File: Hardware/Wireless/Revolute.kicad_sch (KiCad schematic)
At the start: 52 parts, among them U1 BQ27441-G1, U2 Button, U2 nrf52833_qfn40, U3 AS5600, U4 AP2112K-3.3, U5 BQ24075RGT, X1 32.768 kHz, X2 32MHZ

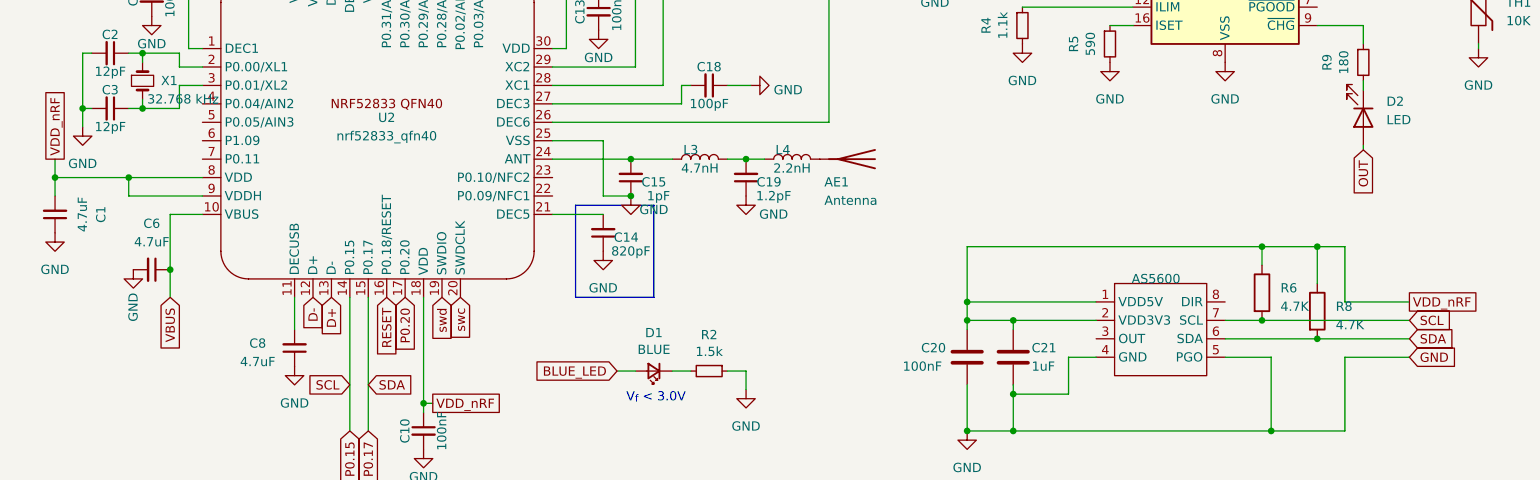
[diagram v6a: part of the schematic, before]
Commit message: fixed debugger datapin board, connected dir and out of as5600 to mcu
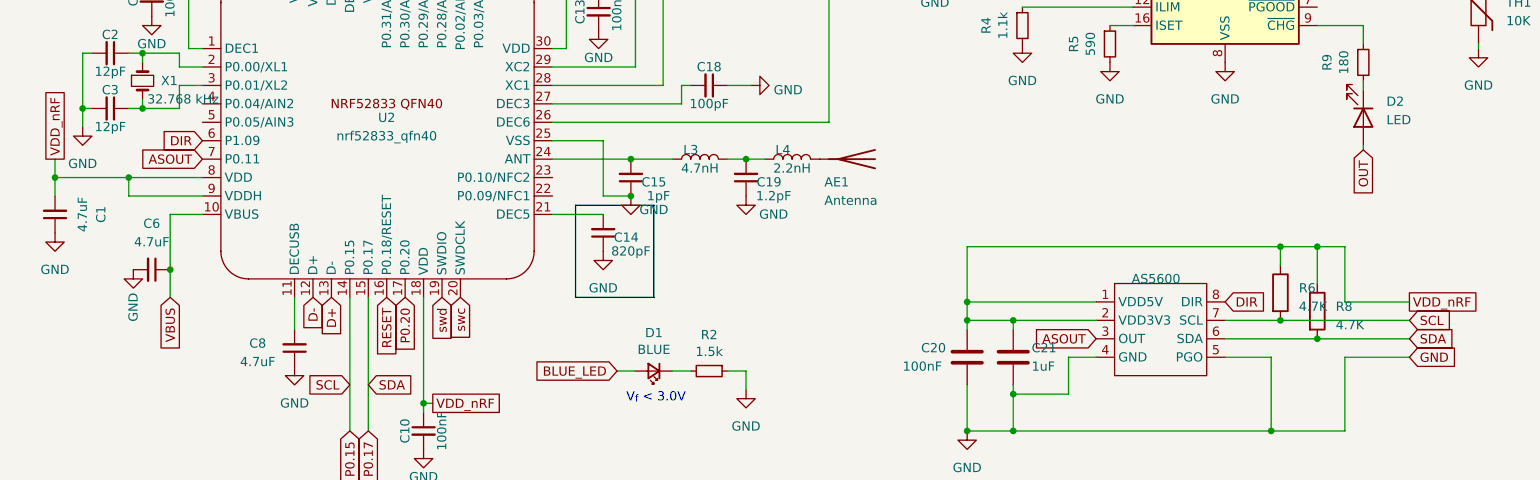
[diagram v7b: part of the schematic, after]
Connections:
- net DIR: now reaches U2.6 (P1.09)
- net DIR: now also U3.8 (DIR)
- net ASOUT: now reaches U2.7 (P0.11)
- net ASOUT: now also U3.3 (OUT)
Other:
- moved on the sheet: R6
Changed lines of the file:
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@@
   (junction (at 25.4 69.215) (diameter 0) (color 0 0 0 0)
   )
-  (junction (at 187.96 98.425) (diameter 0) (color 0 0 0 0)
-  )
   (junction (at 30.48 134.62) (diameter 0) (color 0 0 0 0)
   )
-  (junction (at 187.96 88.265) (diameter 0) (color 0 0 0 0)
+  (junction (at 190.5 98.425) (diameter 0) (color 0 0 0 0)
   )
   (junction (at 100.965 81.28) (diameter 0) (color 0 0 0 0)
@@
   (junction (at 21.59 78.74) (diameter 0) (color 0 0 0 0)
   )
+  (junction (at 190.5 88.265) (diameter 0) (color 0 0 0 0)
+  )
   (junction (at 198.12 140.335) (diameter 0) (color 0 0 0 0)
   )
@@
     (stroke (width 0) (type default))
   )
+  (wire (pts (xy 190.5 88.265) (xy 195.58 88.265))
+    (stroke (width 0) (type default))
+  )
   (wire (pts (xy 90.17 73.66) (xy 97.155 73.66))
     (stroke (width 0) (type default))
@@
     (stroke (width 0) (type default))
   )
-  (wire (pts (xy 187.96 88.265) (xy 187.96 90.805))
+  (wire (pts (xy 190.5 88.265) (xy 190.5 90.805))
     (stroke (width 0) (type default))
   )
@@
     (stroke (width 0) (type default))
   )
-  (wire (pts (xy 187.96 88.265) (xy 195.58 88.265))
-    (stroke (width 0) (type default))
-  )
   (wire (pts (xy 106.68 105.41) (xy 109.22 105.41))
     (stroke (width 0) (type solid))
@@
     (stroke (width 0) (type default))
   )
-  (wire (pts (xy 187.96 98.425) (xy 208.28 98.425))
+  (wire (pts (xy 182.88 98.425) (xy 190.5 98.425))
     (stroke (width 0) (type default))
   )
@@
     (stroke (width 0) (type default))
   )
+  (wire (pts (xy 190.5 98.425) (xy 208.28 98.425))
+    (stroke (width 0) (type default))
+  )
   (wire (pts (xy 73.66 109.855) (xy 72.39 109.855))
     (stroke (width 0) (type default))
@@
     (stroke (width 0) (type default))
   )
-  (wire (pts (xy 147.32 88.265) (xy 187.96 88.265))
+  (wire (pts (xy 147.32 88.265) (xy 190.5 88.265))
     (stroke (width 0) (type default))
   )
@@
     (stroke (width 0) (type default))
   )
-  (wire (pts (xy 182.88 98.425) (xy 187.96 98.425))
-    (stroke (width 0) (type default))
-  )
   (wire (pts (xy 61.595 160.02) (xy 61.595 161.29))
     (stroke (width 0) (type default))
@@
     )
   )
+  (global_label "ASOUT" (shape input) (at 165.1 100.965 180) (fields_autoplaced)
+    (effects (font (size 1.27 1.27)) (justify right))
+    (property "Intersheetrefs" "${INTERSHEET_REFS}" (at 156.2675 100.965 0)
+      (effects (font (size 1.27 1.27)) (justify right) hide)
+    )
+  )
   (global_label "VBUS" (shape input) (at 182.88 28.575 90) (fields_autoplaced)
     (effects (font (size 1.27 1.27)) (justify left))
@@
     )
   )
+  (global_label "DIR" (shape input) (at 41.91 73.66 180) (fields_autoplaced)
+    (effects (font (size 1.27 1.27)) (justify right))
+    (property "Intersheetrefs" "${INTERSHEET_REFS}" (at 35.8594 73.66 0)
+      (effects (font (size 1.27 1.27)) (justify right) hide)
+    )
+  )
   (global_label "VBUS" (shape input) (at 120.015 162.56 90) (fields_autoplaced)
     (effects (font (size 1.27 1.27)) (justify left))
@@
     )
   )
+  (global_label "ASOUT" (shape input) (at 41.91 76.2 180) (fields_autoplaced)
+    (effects (font (size 1.27 1.27)) (justify right))
+    (property "Intersheetrefs" "${INTERSHEET_REFS}" (at 33.0775 76.2 0)
+      (effects (font (size 1.27 1.27)) (justify right) hide)
+    )
+  )
   (global_label "D+" (shape input) (at 59.69 95.25 270) (fields_autoplaced)
     (effects (font (size 1.27 1.27)) (justify right))
@@
     )
   )
+  (global_label "DIR" (shape input) (at 182.88 95.885 0) (fields_autoplaced)
+    (effects (font (size 1.27 1.27)) (justify left))
+    (property "Intersheetrefs" "${INTERSHEET_REFS}" (at 188.9306 95.885 0)
+      (effects (font (size 1.27 1.27)) (justify left) hide)
+    )
+  )
   (global_label "OUT" (shape input) (at 247.015 125.095 180) (fields_autoplaced)
     (effects (font (size 1.27 1.27)) (justify right))
@@
     )
   )
-  (symbol (lib_id "Device:R") (at 187.96 94.615 0) (unit 1)
+  (symbol (lib_id "Device:R") (at 190.5 94.615 0) (unit 1)
     (in_bom yes) (on_board yes) (dnp no) (fields_autoplaced)
-    (property "Reference" "R6" (at 190.5 93.98 0)
+    (property "Reference" "R6" (at 193.04 93.98 0)
       (effects (font (size 1.27 1.27)) (justify left))
     )
-    (property "Value" "4.7K" (at 190.5 96.52 0)
+    (property "Value" "4.7K" (at 193.04 96.52 0)
       (effects (font (size 1.27 1.27)) (justify left))
     )
-    (property "Footprint" "Resistor_SMD:R_0402_1005Metric" (at 186.182 94.615 90)
+    (property "Footprint" "Resistor_SMD:R_0402_1005Metric" (at 188.722 94.615 90)
       (effects (font (size 1.27 1.27)) hide)
     )
-    (property "Datasheet" "~" (at 187.96 94.615 0)
+    (property "Datasheet" "~" (at 190.5 94.615 0)
       (effects (font (size 1.27 1.27)) hide)
     )
